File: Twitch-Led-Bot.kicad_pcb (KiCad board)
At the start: 2 copper layers, 83 x 31.5 mm, 32 parts, among them J1 USB4105-GF-A, Q1 BC847, Q2 BC847, SW1 Reset, U1 AMS1117-3.3, U2 CH340G, U3 ESP-12F, Y1 12MHz

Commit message: Bug correction v.1.0.1
Correction in the wiring diagram with the microcontroller connecting GP015 to GND
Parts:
- D1: value RX -> RX - BLUE
- D2: value TX -> TX - GREEN
- D3: value PW -> PW - YELLOW
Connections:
- U3 pad 16: unconnected-(U3-Pad16) -> GND
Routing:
- net GND: track 179.9 -> 181.9 mm
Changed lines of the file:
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@@
   (net 34 "unconnected-(U3-Pad13)")
   (net 35 "unconnected-(U3-Pad14)")
-  (net 36 "unconnected-(U3-Pad16)")
-  (net 37 "unconnected-(U3-Pad17)")
-  (net 38 "unconnected-(U3-Pad19)")
-  (net 39 "unconnected-(U3-Pad20)")
-  (net 40 "unconnected-(J1-PadA8)")
-  (net 41 "unconnected-(J1-PadB5)")
-  (net 42 "unconnected-(J1-PadA5)")
-  (net 43 "unconnected-(J1-PadB8)")
+  (net 36 "unconnected-(U3-Pad17)")
+  (net 37 "unconnected-(U3-Pad19)")
+  (net 38 "unconnected-(U3-Pad20)")
+  (net 39 "unconnected-(J1-PadA8)")
+  (net 40 "unconnected-(J1-PadB5)")
+  (net 41 "unconnected-(J1-PadA5)")
+  (net 42 "unconnected-(J1-PadB8)")
   (footprint "MountingHole:MountingHole_2.1mm" (layer "F.Cu")
     (at 91.948 71.2724)
@@
       (net 2 "GND") (pinfunction "GND") (pintype "power_in"))
     (pad "16" smd rect (at 7.6 8.5 90) (size 2.5 1) (layers "F.Cu" "F.Paste" "F.Mask")
-      (net 36 "unconnected-(U3-Pad16)") (pinfunction "GPIO15") (pintype "bidirectional+no_connect"))
+      (net 2 "GND") (pinfunction "GPIO15") (pintype "bidirectional"))
     (pad "17" smd rect (at 7.6 6.5 90) (size 2.5 1) (layers "F.Cu" "F.Paste" "F.Mask")
-      (net 37 "unconnected-(U3-Pad17)") (pinfunction "GPIO2") (pintype "bidirectional+no_connect"))
+      (net 36 "unconnected-(U3-Pad17)") (pinfunction "GPIO2") (pintype "bidirectional+no_connect"))
     (pad "18" smd rect (at 7.6 4.5 90) (size 2.5 1) (layers "F.Cu" "F.Paste" "F.Mask")
       (net 16 "IO0") (pinfunction "GPIO0") (pintype "bidirectional"))
     (pad "19" smd rect (at 7.6 2.5 90) (size 2.5 1) (layers "F.Cu" "F.Paste" "F.Mask")
-      (net 38 "unconnected-(U3-Pad19)") (pinfunction "GPIO4") (pintype "bidirectional+no_connect"))
+      (net 37 "unconnected-(U3-Pad19)") (pinfunction "GPIO4") (pintype "bidirectional+no_connect"))
     (pad "20" smd rect (at 7.6 0.5 90) (size 2.5 1) (layers "F.Cu" "F.Paste" "F.Mask")
-      (net 39 "unconnected-(U3-Pad20)") (pinfunction "GPIO5") (pintype "bidirectional+no_connect"))
+      (net 38 "unconnected-(U3-Pad20)") (pinfunction "GPIO5") (pintype "bidirectional+no_connect"))
     (pad "21" smd rect (at 7.6 -1.5 90) (size 2.5 1) (layers "F.Cu" "F.Paste" "F.Mask")
       (net 6 "RX") (pinfunction "GPIO3/RXD") (pintype "bidirectional"))
@@
       (effects (font (size 1 1) (thickness 0.15)))
     )
-    (fp_text value "PW" (at -3.1519 -0.0762) (layer "F.SilkS")
+    (fp_text value "PW - YELLOW" (at -3.1519 -0.0762) (layer "F.SilkS")
       (effects (font (size 1 1) (thickness 0.15)))
     )
@@
       (net 1 "+5V") (pinfunction "VBUS") (pintype "power_in"))
     (pad "A5" smd rect locked (at -1.25 -4.755 90) (size 0.3 1.15) (layers "F.Cu" "F.Paste" "F.Mask")
-      (net 42 "unconnected-(J1-PadA5)") (pinfunction "CC1") (pintype "bidirectional+no_connect"))
+      (net 41 "unconnected-(J1-PadA5)") (pinfunction "CC1") (pintype "bidirectional+no_connect"))
     (pad "A6" smd rect locked (at -0.25 -4.755 90) (size 0.3 1.15) (layers "F.Cu" "F.Paste" "F.Mask")
       (net 18 "D+") (pinfunction "DP1") (pintype "bidirectional"))
@@
       (net 19 "D-") (pinfunction "DN1") (pintype "bidirectional"))
     (pad "A8" smd rect locked (at 1.25 -4.755 90) (size 0.3 1.15) (layers "F.Cu" "F.Paste" "F.Mask")
-      (net 40 "unconnected-(J1-PadA8)") (pinfunction "SBU1") (pintype "bidirectional+no_connect"))
+      (net 39 "unconnected-(J1-PadA8)") (pinfunction "SBU1") (pintype "bidirectional+no_connect"))
     (pad "B1_A12" smd rect locked (at 3.2 -4.755 90) (size 0.6 1.15) (layers "F.Cu" "F.Paste" "F.Mask")
       (net 2 "GND") (pinfunction "GND") (pintype "power_in"))
@@
       (net 1 "+5V") (pinfunction "VBUS") (pintype "power_in"))
     (pad "B5" smd rect locked (at 1.75 -4.755 90) (size 0.3 1.15) (layers "F.Cu" "F.Paste" "F.Mask")
-      (net 41 "unconnected-(J1-PadB5)") (pinfunction "CC2") (pintype "bidirectional+no_connect"))
+      (net 40 "unconnected-(J1-PadB5)") (pinfunction "CC2") (pintype "bidirectional+no_connect"))
     (pad "B6" smd rect locked (at 0.75 -4.755 90) (size 0.3 1.15) (layers "F.Cu" "F.Paste" "F.Mask")
       (net 18 "D+") (pinfunction "DP2") (pintype "bidirectional"))
@@
       (net 19 "D-") (pinfunction "DN2") (pintype "bidirectional"))
     (pad "B8" smd rect locked (at -1.75 -4.755 90) (size 0.3 1.15) (layers "F.Cu" "F.Paste" "F.Mask")
-      (net 43 "unconnected-(J1-PadB8)") (pinfunction "SBU2") (pintype "bidirectional+no_connect"))
+      (net 42 "unconnected-(J1-PadB8)") (pinfunction "SBU2") (pintype "bidirectional+no_connect"))
     (pad "S1" thru_hole oval locked (at -4.32 -4.18 90) (size 1.05 2.1) (drill oval 0.6 1.7) (layers *.Cu *.Mask)
       (net 2 "GND") (pinfunction "SHELL_GND") (pintype "power_in"))
@@
       (effects (font (size 1 1) (thickness 0.15)))
     )
-    (fp_text value "TX" (at 2.8194 0.0508) (layer "F.SilkS")
+    (fp_text value "TX - GREEN" (at 2.8194 0.0508) (layer "F.SilkS")
       (effects (font (size 1 1) (thickness 0.15)))
     )
@@
       (effects (font (size 1 1) (thickness 0.15)))
     )
-    (fp_text value "RX" (at 2.9972 0.0508) (layer "F.SilkS")
+    (fp_text value "RX - BLUE" (at 2.9972 0.0508) (layer "F.SilkS")
       (effects (font (size 1 1) (thickness 0.15)))
     )
@@
   (segment (start 115.2144 74.041) (end 108.9445 74.041) (width 0.25) (layer "F.Cu") (net 2))
   (segment (start 162.2596 87.5927) (end 161.6846 87.0177) (width 0.25) (layer "F.Cu") (net 2))
+  (segment (start 106.8742 75.6866) (end 108.8742 75.6866) (width 0.25) (layer "F.Cu") (net 2))
   (segment (start 108.8742 75.6866) (end 108.8742 74.1113) (width 0.25) (layer "F.Cu") (net 2))
   (segment (start 156.8586 70.8127) (end 155.7752 69.7293) (width 0.25) (layer "F.Cu") (net 2))
@@
     (polygon
       (pts
-        (xy 171.323 66.0908)
-        (xy 170.7896 100.6856)
-        (xy 82.5246 101.4476)
-        (xy 82.6262 66.3194)
-        (xy 171.4246 65.9892)
+        (xy 171.4246 65.786)
+        (xy 170.8912 100.3808)
+        (xy 82.6262 101.1428)
+        (xy 82.7278 66.0146)
+        (xy 171.5262 65.6844)
       )
     )

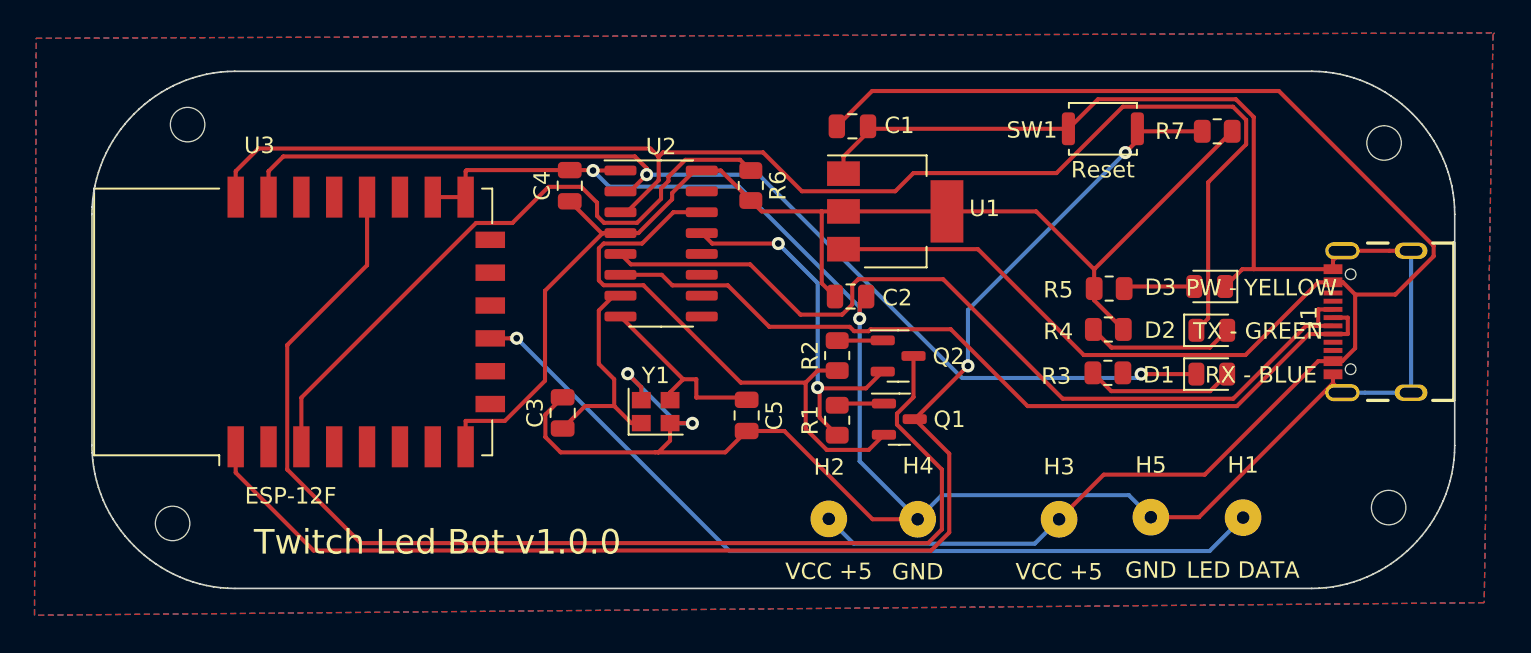
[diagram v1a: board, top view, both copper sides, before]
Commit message: Bug correction v.1.0.2
RX LED has problems on the trail in the schematic
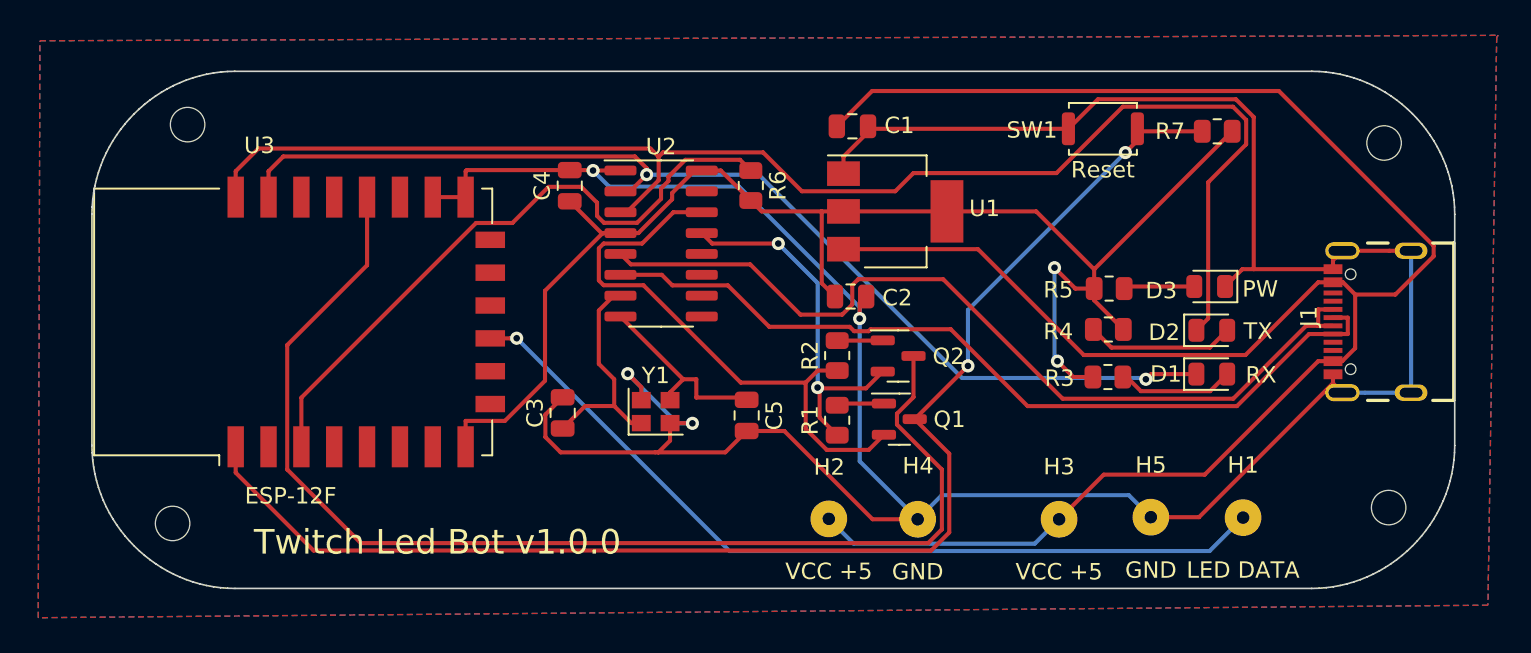
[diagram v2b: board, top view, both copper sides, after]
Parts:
- D1: value RX - BLUE -> RX
- D2: value TX - GREEN -> TX
- D3: value PW - YELLOW -> PW
- moved R3 0.25 mm to (148.0, 86.6), turned to 180 degrees
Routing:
- net +3V3: track 76.7 -> 87.9 mm, vias 0 -> 2
- net Net-(D1-Pad2): track 9.07 -> 7.14 mm
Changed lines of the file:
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@@
   )
   (footprint "Resistor_SMD:R_0805_2012Metric" (layer "F.Cu")
-    (at 147.9804 86.3854)
+    (at 147.9804 86.6394 180)
     (descr "Resistor SMD 0805 (2012 Metric), square (rectangular) end terminal, IPC_7351 nominal, (Body size source: IPC-SM-782 page 72, https://www.pcb-3d.com/wordpress/wp-content/uploads/ipc-sm-782a_amendment_1_and_2.pdf), generated with kicad-footprint-generator")
     (tags "resistor")
@@
     (property "Sheetname" "")
     (attr smd)
-    (fp_text reference "R3" (at -3.1496 0.2032) (layer "F.SilkS")
+    (fp_text reference "R3" (at 2.9464 -0.0762) (layer "F.SilkS")
       (effects (font (size 1 1) (thickness 0.15)))
     )
@@
     (fp_line (start -1 -0.625) (end 1 -0.625) (layer "F.Fab") (width 0.1))
     (fp_line (start -1 0.625) (end -1 -0.625) (layer "F.Fab") (width 0.1))
-    (pad "1" smd roundrect (at -0.9125 0) (size 1.025 1.4) (layers "F.Cu" "F.Paste" "F.Mask") (roundrect_rratio 0.243902439)
+    (pad "1" smd roundrect (at -0.9125 0 180) (size 1.025 1.4) (layers "F.Cu" "F.Paste" "F.Mask") (roundrect_rratio 0.243902439)
       (net 7 "Net-(D1-Pad2)") (pintype "passive"))
-    (pad "2" smd roundrect (at 0.9125 0) (size 1.025 1.4) (layers "F.Cu" "F.Paste" "F.Mask") (roundrect_rratio 0.243902439)
+    (pad "2" smd roundrect (at 0.9125 0 180) (size 1.025 1.4) (layers "F.Cu" "F.Paste" "F.Mask") (roundrect_rratio 0.243902439)
       (net 3 "+3V3") (pintype "passive"))
     (model "${KICAD6_3DMODEL_DIR}/Resistor_SMD.3dshapes/R_0805_2012Metric.wrl"
@@
     (property "Sheetname" "")
     (attr smd)
-    (fp_text reference "D3" (at 2.9972 -0.0508) (layer "F.SilkS")
-      (effects (font (size 1 1) (thickness 0.15)))
-    )
-    (fp_text value "PW - YELLOW" (at -3.1519 -0.0762) (layer "F.SilkS")
+    (fp_text reference "D3" (at 2.9441 -0.254) (layer "F.SilkS")
+      (effects (font (size 1 1) (thickness 0.15)))
+    )
+    (fp_text value "PW" (at -3.0757 -0.1524) (layer "F.SilkS")
       (effects (font (size 1 1) (thickness 0.15)))
     )
@@
     (property "Sheetname" "")
     (attr smd)
-    (fp_text reference "D2" (at -3.1496 0) (layer "F.SilkS")
-      (effects (font (size 1 1) (thickness 0.15)))
-    )
-    (fp_text value "TX - GREEN" (at 2.8194 0.0508) (layer "F.SilkS")
+    (fp_text reference "D2" (at -2.8956 0.127) (layer "F.SilkS")
+      (effects (font (size 1 1) (thickness 0.15)))
+    )
+    (fp_text value "TX" (at 2.8194 0.0508) (layer "F.SilkS")
       (effects (font (size 1 1) (thickness 0.15)))
     )
@@
     (property "Sheetname" "")
     (attr smd)
-    (fp_text reference "D1" (at -3.2258 0.0508) (layer "F.SilkS")
-      (effects (font (size 1 1) (thickness 0.15)))
-    )
-    (fp_text value "RX - BLUE" (at 2.9972 0.0508) (layer "F.SilkS")
+    (fp_text reference "D1" (at -2.794 0) (layer "F.SilkS")
+      (effects (font (size 1 1) (thickness 0.15)))
+    )
+    (fp_text value "RX" (at 2.9972 0.0508) (layer "F.SilkS")
       (effects (font (size 1 1) (thickness 0.15)))
     )
@@
   (segment (start 125.5194 75.0439) (end 132.865 82.3895) (width 0.25) (layer "B.Cu") (net 2))
   (segment (start 124.4111 74.0664) (end 123.252 74.0664) (width 0.25) (layer "F.Cu") (net 3))
+  (segment (start 145.9992 81.2546) (end 144.7292 79.9846) (width 0.25) (layer "F.Cu") (net 3))
   (segment (start 147.1441 81.9677) (end 148.9202 83.7438) (width 0.25) (layer "F.Cu") (net 3))
   (segment (start 117.2218 77.8764) (end 117.1858 77.9124) (width 0.25) (layer "F.Cu") (net 3))
@@
   (segment (start 155.5496 71.6788) (end 147.1441 80.0843) (width 0.25) (layer "F.Cu") (net 3))
   (segment (start 138.181 76.5556) (end 131.881 76.5556) (width 0.25) (layer "F.Cu") (net 3))
+  (segment (start 147.0679 86.6394) (end 145.8722 86.6394) (width 0.25) (layer "F.Cu") (net 3))
   (segment (start 130.5556 80.9296) (end 131.3632 81.7372) (width 0.25) (layer "F.Cu") (net 3))
+  (segment (start 147.1441 81.2546) (end 145.9992 81.2546) (width 0.25) (layer "F.Cu") (net 3))
   (segment (start 138.181 76.5556) (end 143.6154 76.5556) (width 0.25) (layer "F.Cu") (net 3))
   (segment (start 126.9003 76.5556) (end 126.238 75.8933) (width 0.25) (layer "F.Cu") (net 3))
@@
   (segment (start 119.3902 77.8764) (end 118.302 77.8764) (width 0.25) (layer "F.Cu") (net 3))
   (segment (start 113.7088 86.8676) (end 111.2651 89.3113) (width 0.25) (layer "F.Cu") (net 3))
+  (segment (start 145.8722 86.6394) (end 144.907 85.6742) (width 0.25) (layer "F.Cu") (net 3))
   (segment (start 122.817 74.0664) (end 121.449 75.4344) (width 0.25) (layer "F.Cu") (net 3))
   (segment (start 108.8742 90.8866) (end 108.8742 89.3113) (width 0.25) (layer "F.Cu") (net 3))
@@
   (segment (start 113.7088 81.3894) (end 113.7088 86.8676) (width 0.25) (layer "F.Cu") (net 3))
   (segment (start 118.302 77.8764) (end 117.2218 77.8764) (width 0.25) (layer "F.Cu") (net 3))
+  (via (at 144.907 85.6742) (size 0.8) (drill 0.4) (layers "F.Cu" "B.Cu") (net 3))
+  (via (at 144.7292 79.9846) (size 0.8) (drill 0.4) (layers "F.Cu" "B.Cu") (net 3))
+  (segment (start 144.7292 85.4964) (end 144.907 85.6742) (width 0.25) (layer "B.Cu") (net 3))
+  (segment (start 144.7292 79.9846) (end 144.7292 85.4964) (width 0.25) (layer "B.Cu") (net 3))
   (segment (start 119.5718 89.4476) (end 118.9624 89.4476) (width 0.25) (layer "F.Cu") (net 4))
   (segment (start 116.1498 88.4066) (end 114.7826 89.7738) (width 0.25) (layer "F.Cu") (net 4))
@@
   (segment (start 122.1219 86.7763) (end 118.302 82.9564) (width 0.25) (layer "F.Cu") (net 5))
   (segment (start 122.9214 87.8889) (end 125.8467 87.8889) (width 0.25) (layer "F.Cu") (net 5))
+  (segment (start 153.3675 86.4616) (end 150.6069 86.4616) (width 0.25) (layer "F.Cu") (net 6))
   (segment (start 119.9013 74.3186) (end 119.9013 73.9325) (width 0.25) (layer "F.Cu") (net 6))
   (segment (start 96.8742 75.6866) (end 96.8742 74.1113) (width 0.25) (layer "F.Cu") (net 6))
-  (segment (start 153.3675 86.4616) (end 150.0071 86.4616) (width 0.25) (layer "F.Cu") (net 6))
   (segment (start 118.8835 75.3364) (end 119.9013 74.3186) (width 0.25) (layer "F.Cu") (net 6))
   (segment (start 118.302 75.3364) (end 118.8835 75.3364) (width 0.25) (layer "F.Cu") (net 6))
   (segment (start 119.1795 73.2107) (end 97.7748 73.2107) (width 0.25) (layer "F.Cu") (net 6))
+  (segment (start 150.6069 86.4616) (end 150.2918 86.7767) (width 0.25) (layer "F.Cu") (net 6))
   (segment (start 119.9013 73.9325) (end 119.1795 73.2107) (width 0.25) (layer "F.Cu") (net 6))
   (segment (start 97.7748 73.2107) (end 96.8742 74.1113) (width 0.25) (layer "F.Cu") (net 6))
   (via (at 119.9013 74.3186) (size 0.8) (drill 0.4) (layers "F.Cu" "B.Cu") (net 6))
-  (via (at 150.0071 86.4616) (size 0.8) (drill 0.4) (layers "F.Cu" "B.Cu") (net 6))
+  (via (at 150.2918 86.7767) (size 0.8) (drill 0.4) (layers "F.Cu" "B.Cu") (net 6))
+  (segment (start 139.1014 86.6972) (end 126.7228 74.3186) (width 0.25) (layer "B.Cu") (net 6))
+  (segment (start 150.2123 86.6972) (end 139.1014 86.6972) (width 0.25) (layer "B.Cu") (net 6))
+  (segment (start 150.2918 86.7767) (end 150.2123 86.6972) (width 0.25) (layer "B.Cu") (net 6))
   (segment (start 126.7228 74.3186) (end 119.9013 74.3186) (width 0.25) (layer "B.Cu") (net 6))
-  (segment (start 149.7715 86.6972) (end 139.1014 86.6972) (width 0.25) (layer "B.Cu") (net 6))
-  (segment (start 139.1014 86.6972) (end 126.7228 74.3186) (width 0.25) (layer "B.Cu") (net 6))
-  (segment (start 150.0071 86.4616) (end 149.7715 86.6972) (width 0.25) (layer "B.Cu") (net 6))
-  (segment (start 148.1837 87.5012) (end 147.0679 86.3854) (width 0.25) (layer "F.Cu") (net 7))
-  (segment (start 154.2029 87.5012) (end 148.1837 87.5012) (width 0.25) (layer "F.Cu") (net 7))
+  (segment (start 149.129195 86.6394) (end 148.8929 86.6394) (width 0.25) (layer "F.Cu") (net 7))
+  (segment (start 149.990995 87.5012) (end 149.129195 86.6394) (width 0.25) (layer "F.Cu") (net 7))
   (segment (start 155.2425 86.4616) (end 154.2029 87.5012) (width 0.25) (layer "F.Cu") (net 7))
+  (segment (start 154.2029 87.5012) (end 149.990995 87.5012) (width 0.25) (layer "F.Cu") (net 7))
   (segment (start 120.8922 72.9637) (end 120.6283 73.2276) (width 0.25) (layer "F.Cu") (net 8))
   (segment (start 148.8918 70.1797) (end 144.8494 74.2221) (width 0.25) (layer "F.Cu") (net 8))
@@
     (polygon
       (pts
-        (xy 171.4246 65.786)
-        (xy 170.8912 100.3808)
-        (xy 82.6262 101.1428)
-        (xy 82.7278 66.0146)
-        (xy 171.5262 65.6844)
+        (xy 171.651874 65.937439)
+        (xy 171.118474 100.532239)
+        (xy 82.853474 101.294239)
+        (xy 82.955074 66.166039)
+        (xy 171.753474 65.835839)
       )
     )
